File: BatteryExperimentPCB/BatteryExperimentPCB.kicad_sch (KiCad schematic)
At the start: 32 parts, among them J1 USB_C_Receptacle_USB2.0_14P, J2 Conn_01x12_Pin, J3 Conn_01x12_Pin, Q1 DMG1012T, SW1 SW_Push, U1 ATtiny3226-M, U2 USBLC6-2P6, U3 BQ25628RYKR

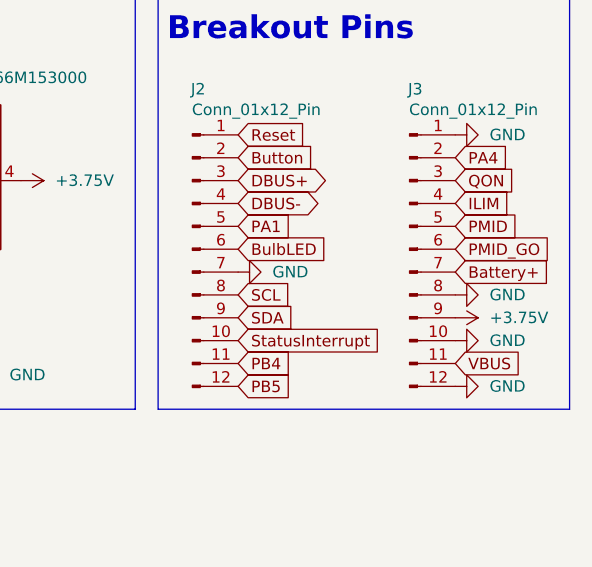
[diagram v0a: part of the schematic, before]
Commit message: pcb layout attempt with components on top and bottom of a two layer pcb, no ground connections yet
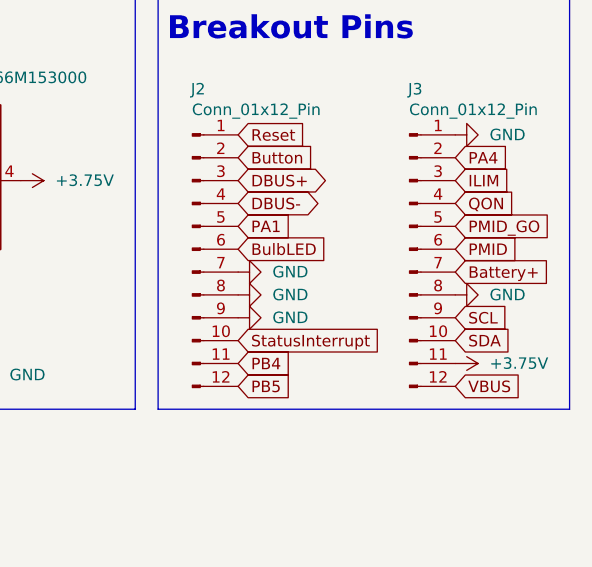
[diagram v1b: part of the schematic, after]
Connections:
- net +3.75V: now also J3.11 (Pin_11); no longer J3.9 (Pin_9)
- net GND: now also J2.8 (Pin_8), J2.9 (Pin_9); no longer J3.10 (Pin_10), J3.12 (Pin_12)
- net ILIM: now also J3.3 (Pin_3); no longer J3.4 (Pin_4)
- net PMID: now also J3.6 (Pin_6); no longer J3.5 (Pin_5)
- net PMID_GO: now also J3.5 (Pin_5); no longer J3.6 (Pin_6)
- net QON: now also J3.4 (Pin_4); no longer J3.3 (Pin_3)
- net SCL: now also J3.9 (Pin_9); no longer J2.8 (Pin_8)
- net SDA: now also J3.10 (Pin_10); no longer J2.9 (Pin_9)
- net VBUS: now also J3.12 (Pin_12); no longer J3.11 (Pin_11)

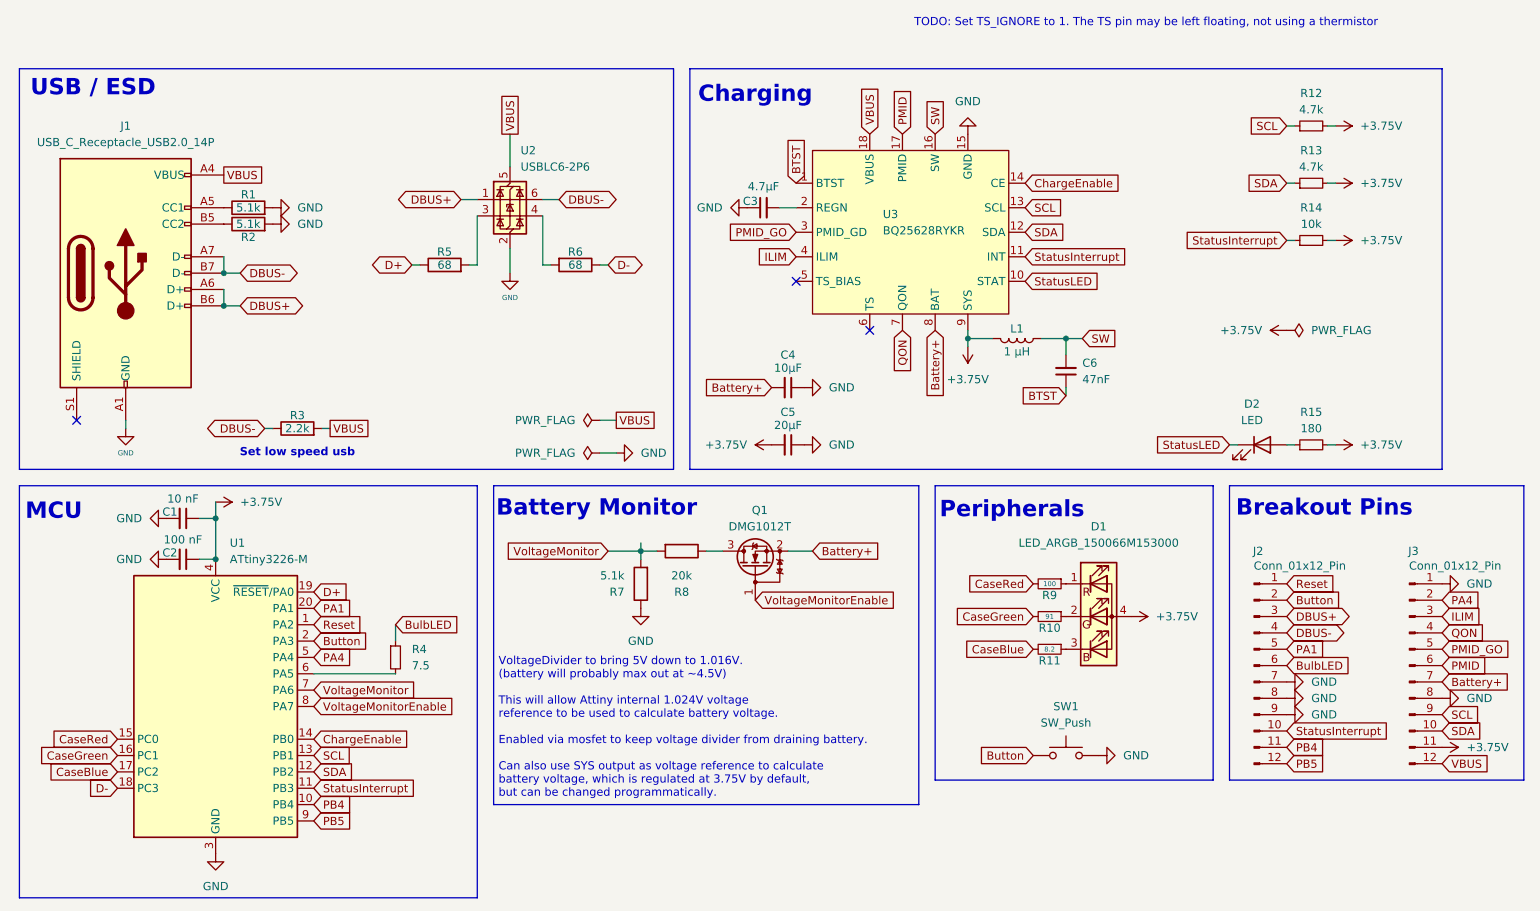
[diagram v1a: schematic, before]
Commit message: second attempt at pcb design, smaller, using ground zones now
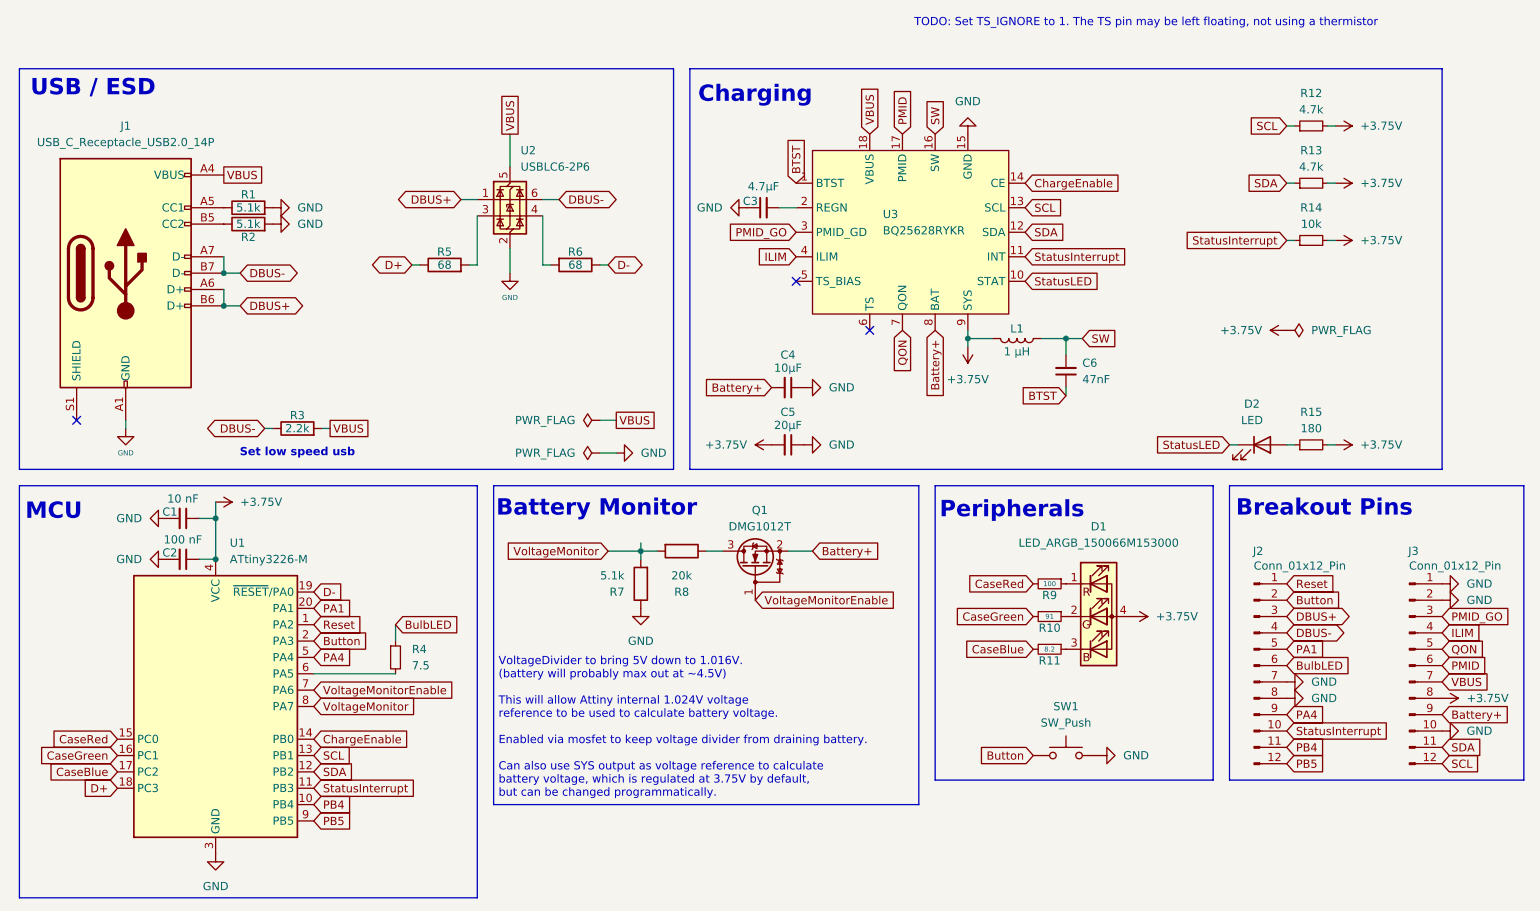
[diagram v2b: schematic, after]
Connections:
- net +3.75V: now also J3.8 (Pin_8); no longer J3.11 (Pin_11)
- net Battery+: now also J3.9 (Pin_9); no longer J3.7 (Pin_7)
- net D+: now also U1.18 (PC3); no longer U1.19 (~{RESET}/PA0)
- net D-: now also U1.19 (~{RESET}/PA0); no longer U1.18 (PC3)
- net GND: now also J3.10 (Pin_10), J3.2 (Pin_2); no longer J2.9 (Pin_9), J3.8 (Pin_8)
- net ILIM: now also J3.4 (Pin_4); no longer J3.3 (Pin_3)
- net PA4: now also J2.9 (Pin_9); no longer J3.2 (Pin_2)
- net PMID_GO: now also J3.3 (Pin_3); no longer J3.5 (Pin_5)
- net QON: now also J3.5 (Pin_5); no longer J3.4 (Pin_4)
- net SCL: now also J3.12 (Pin_12); no longer J3.9 (Pin_9)
- net SDA: now also J3.11 (Pin_11); no longer J3.10 (Pin_10)
- net VBUS: now also J3.7 (Pin_7); no longer J3.12 (Pin_12)
- net VoltageMonitor: now also U1.8 (PA7); no longer U1.7 (PA6)
- net VoltageMonitorEnable: now also U1.7 (PA6); no longer U1.8 (PA7)

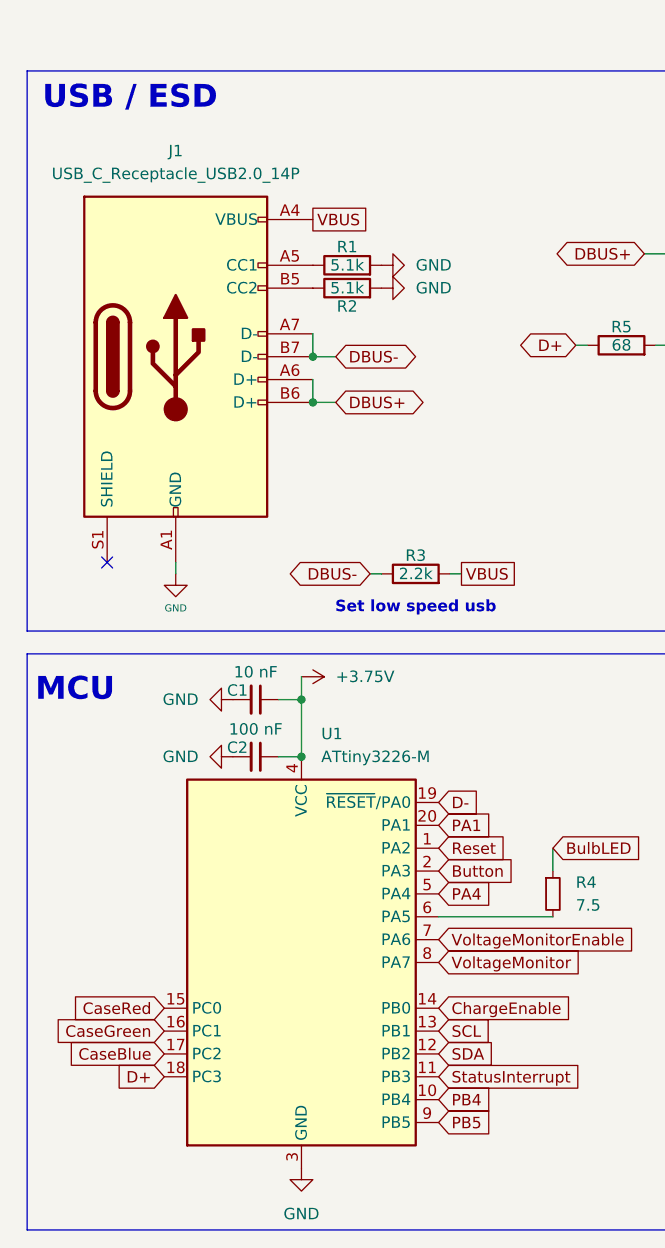
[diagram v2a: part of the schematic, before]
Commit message: redo pcb with components on single side, imported usb rohan uses
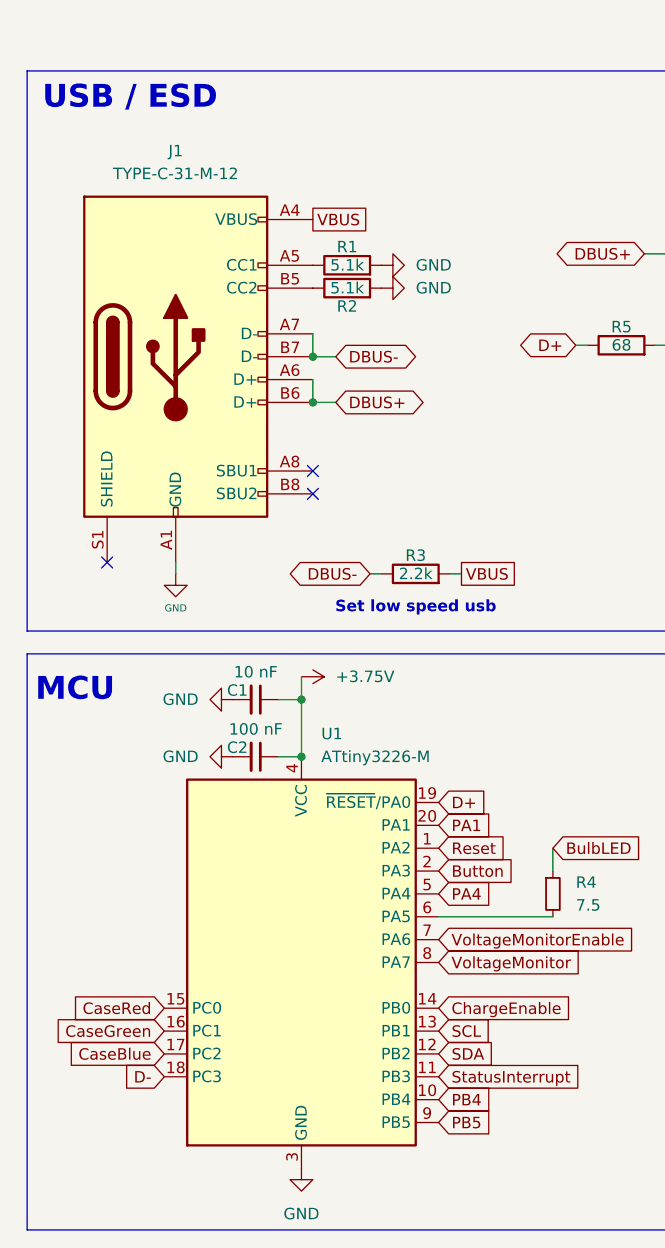
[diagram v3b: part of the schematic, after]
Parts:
- removed J1: USB_C_Receptacle_USB2.0_14P, Connector_USB:USB_C_Receptacle_G-Switch_GT-USB-7025, symbol Connector:USB_C_Receptacle_USB2.0_14P
- added J1: TYPE-C-31-M-12, BatteryExperimentPCB:USB_C_Receptacle_Hroparts_TYPE-C-31-M-12, symbol type-c-31-m-12:TYPE-C-31-M-12
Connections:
- net D+: now also U1.19 (~{RESET}/PA0); no longer U1.18 (PC3)
- net D-: now also U1.18 (PC3); no longer U1.19 (~{RESET}/PA0)
- net DBUS+: now also J1.A6 (D+), J1.B6 (D+)
- net DBUS-: now also J1.A7 (D-), J1.B7 (D-)
- net GND: now also J1.A1 (GND), J1.B1 (GND)
- net VBUS: now also J1.A4 (VBUS), J1.B4 (VBUS)
- net at R1.1: now also J1.A5 (CC1)
- net at R2.1: now also J1.B5 (CC2)
- no-connect marks 3 -> 5
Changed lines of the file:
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@@
 	(paper "A4")
 	(junction
-		(at 176.53 55.88)
+		(at 45.72 45.72)
 		(diameter 0)
 		(color 0 0 0 0)
 	)
 	(junction
-		(at 45.72 50.8)
+		(at 176.53 55.88)
 		(diameter 0)
 		(color 0 0 0 0)
@@
 	)
 	(junction
-		(at 44.45 90.17)
+		(at 45.72 50.8)
 		(diameter 0)
 		(color 0 0 0 0)
 	)
 	(junction
-		(at 45.72 45.72)
+		(at 44.45 90.17)
 		(diameter 0)
 		(color 0 0 0 0)
@@
 	)
 	(no_connect
+		(at 45.72 60.96)
+	)
+	(no_connect
+		(at 45.72 58.42)
+	)
+	(no_connect
 		(at 146.05 54.61)
 	)
@@
 		)
 	)
-	(global_label "D+"
-		(shape input)
-		(at 29.21 125.73 180)
-		(fields_autoplaced yes)
-		(effects
-			(font
-				(size 1.27 1.27)
-			)
-			(justify right)
-		)
-		(property "Intersheetrefs" "${INTERSHEET_REFS}"
-			(at 23.3824 125.73 0)
-			(effects
-				(font
-					(size 1.27 1.27)
-				)
-				(justify right)
-				(hide yes)
-			)
-		)
-	)
 	(global_label "Button"
 		(shape input)
@@
 		)
 	)
+	(global_label "D+"
+		(shape input)
+		(at 59.69 95.25 0)
+		(fields_autoplaced yes)
+		(effects
+			(font
+				(size 1.27 1.27)
+			)
+			(justify left)
+		)
+		(property "Intersheetrefs" "${INTERSHEET_REFS}"
+			(at 65.5176 95.25 0)
+			(effects
+				(font
+					(size 1.27 1.27)
+				)
+				(justify left)
+				(hide yes)
+			)
+		)
+	)
 	(global_label "StatusInterrupt"
 		(shape input)
@@
 		)
 	)
+	(global_label "D-"
+		(shape input)
+		(at 29.21 125.73 180)
+		(fields_autoplaced yes)
+		(effects
+			(font
+				(size 1.27 1.27)
+			)
+			(justify right)
+		)
+		(property "Intersheetrefs" "${INTERSHEET_REFS}"
+			(at 23.3824 125.73 0)
+			(effects
+				(font
+					(size 1.27 1.27)
+				)
+				(justify right)
+				(hide yes)
+			)
+		)
+	)
 	(global_label "PB4"
 		(shape input)
@@
 		)
 	)
-	(global_label "D-"
-		(shape input)
-		(at 59.69 95.25 0)
-		(fields_autoplaced yes)
-		(effects
-			(font
-				(size 1.27 1.27)
-			)
-			(justify left)
-		)
-		(property "Intersheetrefs" "${INTERSHEET_REFS}"
-			(at 65.5176 95.25 0)
-			(effects
-				(font
-					(size 1.27 1.27)
-				)
-				(justify left)
-				(hide yes)
-			)
-		)
-	)
 	(global_label "ChargeEnable"
 		(shape input)
@@
 		(dnp no)
 		(fields_autoplaced yes)
-		(property "Reference" "#PWR027"
+		(property "Reference" "#PWR026"
 			(at 241.3 93.98 0)
 			(effects
@@
 			(project "BatteryExperimentPCB"
 				(path "/057a57c5-fa69-4f68-8ff5-75480ccd2fb3"
-					(reference "#PWR027")
+					(reference "#PWR026")
 					(unit 1)
 				)
@@
 	)
 	(symbol
+		(lib_id "type-c-31-m-12:TYPE-C-31-M-12")
+		(at 30.48 46.99 0)
+		(unit 1)
+		(exclude_from_sim no)
+		(in_bom yes)
+		(on_board yes)
+		(dnp no)
+		(fields_autoplaced yes)
+		(property "Reference" "J1"
+			(at 30.48 22.86 0)
+			(effects
+				(font
+					(size 1.27 1.27)
+				)
+			)
+		)
+		(property "Value" "TYPE-C-31-M-12"
+			(at 30.48 25.4 0)
+			(effects
+				(font
+					(size 1.27 1.27)
+				)
+			)
+		)
+		(property "Footprint" "BatteryExperimentPCB:USB_C_Receptacle_Hroparts_TYPE-C-31-M-12"
+			(at 17.145 45.72 90)
+			(effects
+				(font
+					(size 1.27 1.27)
+				)
+				(hide yes)
+			)
+		)
+		(property "Datasheet" ""
+			(at 34.925 45.72 0)
+			(effects
+				(font
+					(size 1.27 1.27)
+				)
+				(hide yes)
+			)
+		)
+		(property "Description" ""
+			(at 30.48 46.99 0)
+			(effects
+				(font
+					(size 1.27 1.27)
+				)
+				(hide yes)
+			)
+		)
+		(pin "A4"
+		)
+		(pin "A5"
+		)
+		(pin "A7"
+		)
+		(pin "B5"
+		)
+		(pin "B6"
+		)
+		(pin "B7"
+		)
+		(pin "A8"
+		)
+		(pin "A6"
+		)
+		(pin "B1"
+		)
+		(pin "S1"
+		)
+		(pin "B8"
+		)
+		(pin "A1"
+		)
+		(pin "B4"
+		)
+		(instances
+			(project ""
+				(path "/057a57c5-fa69-4f68-8ff5-75480ccd2fb3"
+					(reference "J1")
+					(unit 1)
+				)
+			)
+		)
+	)
+	(symbol
 		(lib_id "power:GND")
 		(at 234.95 116.84 90)
@@
 		(on_board yes)
 		(dnp no)
-		(property "Reference" "#PWR028"
+		(property "Reference" "#PWR029"
 			(at 241.3 116.84 0)
 			(effects
@@
 			(project "BatteryExperimentPCB"
 				(path "/057a57c5-fa69-4f68-8ff5-75480ccd2fb3"
-					(reference "#PWR028")
+					(reference "#PWR029")
 					(unit 1)
 				)
@@
 		(dnp no)
 		(fields_autoplaced yes)
-		(property "Reference" "#PWR026"
+		(property "Reference" "#PWR025"
 			(at 214.63 72.39 0)
 			(effects
@@
 			(project "BatteryExperimentPCB"
 				(path "/057a57c5-fa69-4f68-8ff5-75480ccd2fb3"
-					(reference "#PWR026")
+					(reference "#PWR025")
 					(unit 1)
 				)
@@
 	)
 	(symbol
-		(lib_id "Connector:USB_C_Receptacle_USB2.0_14P")
-		(at 30.48 45.72 0)
-		(unit 1)
-		(exclude_from_sim no)
-		(in_bom yes)
-		(on_board yes)
-		(dnp no)
-		(fields_autoplaced yes)
-		(property "Reference" "J1"
-			(at 30.48 22.86 0)
-			(effects
-				(font
-					(size 1.27 1.27)
-				)
-			)
-		)
-		(property "Value" "USB_C_Receptacle_USB2.0_14P"
-			(at 30.48 25.4 0)
-			(effects
-				(font
-					(size 1.27 1.27)
-				)
-			)
-		)
-		(property "Footprint" "Connector_USB:USB_C_Receptacle_G-Switch_GT-USB-7025"
-			(at 34.29 45.72 0)
-			(effects
-				(font
-					(size 1.27 1.27)
-				)
-				(hide yes)
-			)
-		)
-		(property "Datasheet" "https://www.usb.org/sites/default/files/documents/usb_type-c.zip"
-			(at 34.29 45.72 0)
-			(effects
-				(font
-					(size 1.27 1.27)
-				)
-				(hide yes)
-			)
-		)
-		(property "Description" "USB 2.0-only 14P Type-C Receptacle connector"
-			(at 30.48 45.72 0)
-			(effects
-				(font
-					(size 1.27 1.27)
-				)
-				(hide yes)
-			)
-		)
-		(pin "A1"
-		)
-		(pin "B12"
-		)
-		(pin "B4"
-		)
-		(pin "S1"
-		)
-		(pin "B7"
-		)
-		(pin "B6"
-		)
-		(pin "B5"
-		)
-		(pin "A9"
-		)
-		(pin "A4"
-		)
-		(pin "A5"
-		)
-		(pin "A6"
-		)
-		(pin "A7"
-		)
-		(pin "A12"
-		)
-		(pin "B9"
-		)
-		(pin "B1"
-		)
-		(instances
-			(project "BatteryExperimentPCB"
-				(path "/057a57c5-fa69-4f68-8ff5-75480ccd2fb3"
-					(reference "J1")
-					(unit 1)
-				)
-			)
-		)
-	)
-	(symbol
 		(lib_id "power:GND")
 		(at 161.29 24.13 180)
@@
 		(dnp no)
 		(fields_autoplaced yes)
-		(property "Reference" "#PWR022"
+		(property "Reference" "#PWR027"
 			(at 241.3 96.52 0)
 			(effects
@@
 			(project "BatteryExperimentPCB"
 				(path "/057a57c5-fa69-4f68-8ff5-75480ccd2fb3"
-					(reference "#PWR022")
+					(reference "#PWR027")
 					(unit 1)
 				)
@@
 		(dnp no)
 		(fields_autoplaced yes)
-		(property "Reference" "#PWR023"
+		(property "Reference" "#PWR022"
 			(at 214.63 22.86 0)
 			(effects
@@
 			(project "BatteryExperimentPCB"
 				(path "/057a57c5-fa69-4f68-8ff5-75480ccd2fb3"
-					(reference "#PWR023")
+					(reference "#PWR022")
 					(unit 1)
 				)
@@
 		(dnp no)
 		(fields_autoplaced yes)
-		(property "Reference" "#PWR025"
+		(property "Reference" "#PWR024"
 			(at 214.63 40.64 0)
 			(effects
@@
 			(project "BatteryExperimentPCB"
 				(path "/057a57c5-fa69-4f68-8ff5-75480ccd2fb3"
-					(reference "#PWR025")
+					(reference "#PWR024")
 					(unit 1)
 				)
@@
 		(dnp no)
 		(fields_autoplaced yes)
-		(property "Reference" "#PWR029"
+		(property "Reference" "#PWR028"
 			(at 231.14 111.76 0)
 			(effects
@@
 			(project "BatteryExperimentPCB"
 				(path "/057a57c5-fa69-4f68-8ff5-75480ccd2fb3"
-					(reference "#PWR029")
+					(reference "#PWR028")
 					(unit 1)
 				)
@@
 		(dnp no)
 		(fields_autoplaced yes)
-		(property "Reference" "#PWR024"
+		(property "Reference" "#PWR023"
 			(at 214.63 31.75 0)
 			(effects
@@
 			(project "BatteryExperimentPCB"
 				(path "/057a57c5-fa69-4f68-8ff5-75480ccd2fb3"
-					(reference "#PWR024")
+					(reference "#PWR023")
 					(unit 1)
 				)
